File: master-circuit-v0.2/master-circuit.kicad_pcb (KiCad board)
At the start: 4 copper layers, 70 x 86 mm, 254 parts, among them U6 20nF 5%, X2 24MHz

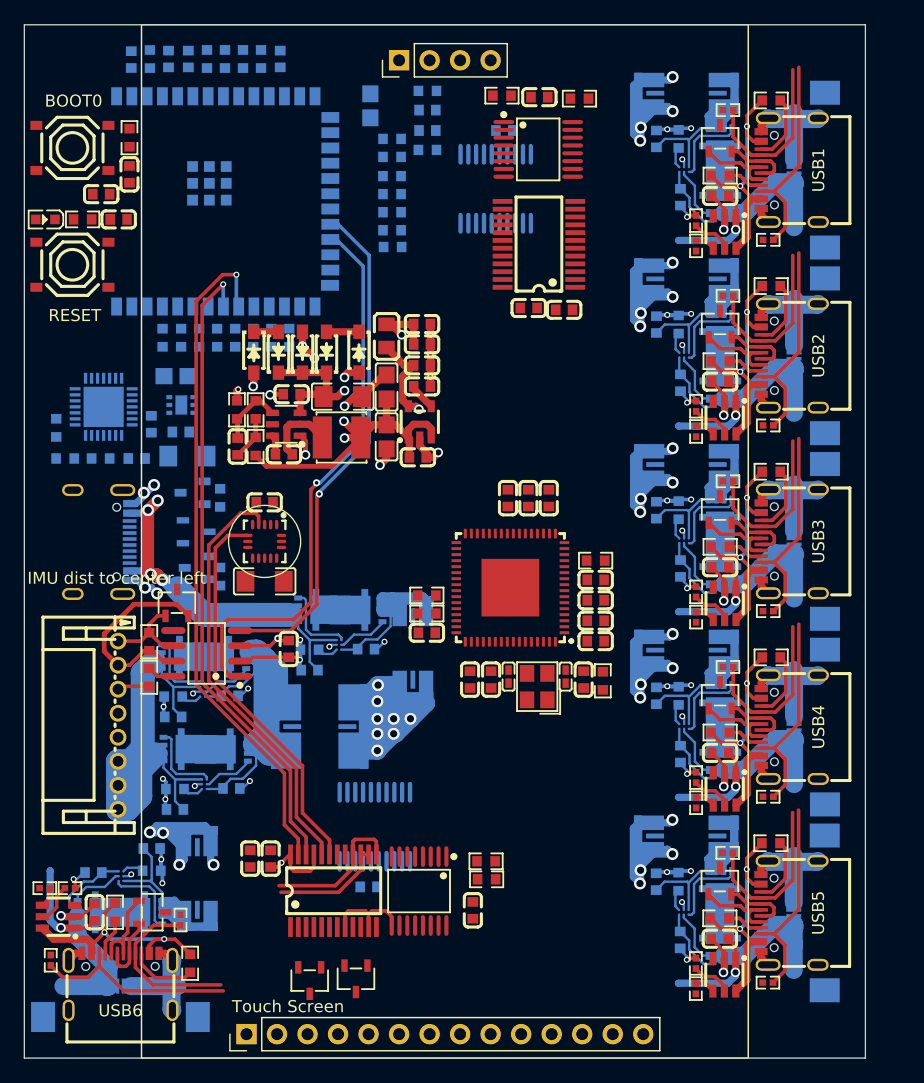
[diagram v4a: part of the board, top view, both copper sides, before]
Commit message: Deal with most of the connection spider web, connector lines remaining.
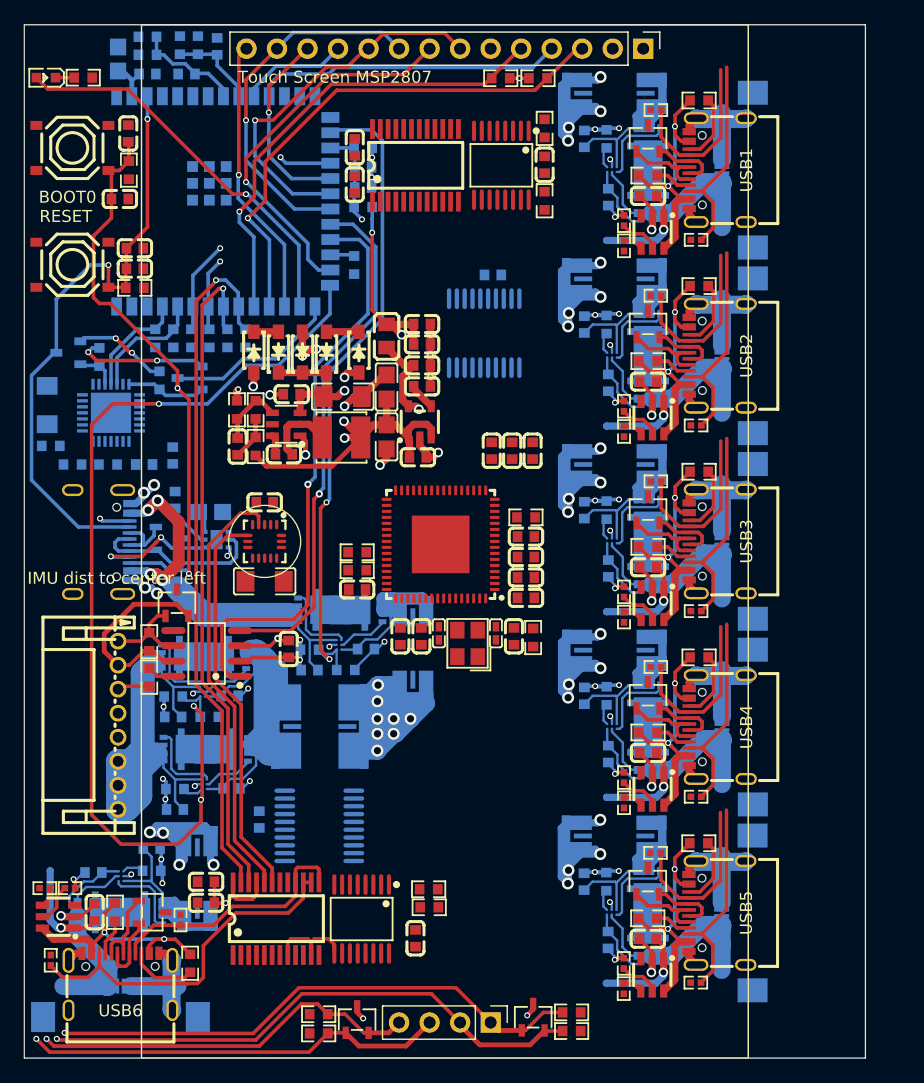
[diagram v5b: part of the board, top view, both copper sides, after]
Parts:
- C1, R14, R15, R26, R27, R34, R37, R9: moved to F.Cu
- moved R9 72.8 mm to (145.6, 139.2)
- moved R34 72.7 mm to (145.6, 140.8)
- moved R15 68.6 mm to (124.5, 140.9), turned to 180 degrees
- moved R14 68.5 mm to (124.5, 139.3), turned to 180 degrees
- moved R12 44.4 mm to (126.8, 110.7)
- moved R11 42.0 mm to (115.4, 114.6)
- moved R27 29.9 mm to (142.8, 61.5), turned to 180 degrees
- moved R26 28.8 mm to (139.7, 61.5), turned to 0 degrees
- moved C3 21.4 mm to (107.8, 59.9), turned to -90 degrees
- moved C84 20.3 mm to (127.5, 70.3), turned to -90 degrees
- moved C42 19.7 mm to (127.5, 67.2), turned to 90 degrees
- moved R37 19.1 mm to (109.2, 78.9), turned to 0 degrees
- moved C1 17.7 mm to (109.2, 77.3), turned to 180 degrees
- moved R43 17.1 mm to (111.2, 86.6)
- moved Q10 15.8 mm to (113.8, 86.4)
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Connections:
- net Net-(Q10-B) renamed /RTS-GATE
- net Net-(Q9-B) renamed /DTR-GATE
- net Net-(U5-VSET) renamed /USB-PD-VSET
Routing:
- net FSPID/SPI2_MOSI: track 0.00 -> 169.5 mm, vias 0 -> 2
- net FSPIQ/SPI2_MISO: track 0.00 -> 154.8 mm, vias 0 -> 2
- net FSPICLK/SPI2_CLK: track 0.00 -> 153.3 mm, vias 0 -> 2
- net FSPICS0/MEMORY_CS: track 0.00 -> 138.4 mm, vias 0 -> 2
- net CONNECT_BATTERY: track 3.57 -> 86.6 mm, vias 0 -> 3
- net BOOT0: track 0.00 -> 62.5 mm, vias 0 -> 2
- net CONNECT_VBUS: track 1.79 -> 55.1 mm, vias 0 -> 2
- net ENABLE-ESP32: track 0.00 -> 51.3 mm, vias 0 -> 2
- net SCREEN_CS: track 0.00 -> 44.2 mm, vias 0 -> 1
- net SCREEN_DC: track 0.00 -> 39.3 mm, vias 0 -> 1
- net STATUS_LED: track 0.00 -> 32.8 mm, vias 0 -> 1
- net SCREEN_LED: track 0.00 -> 31.9 mm, vias 0 -> 1
- net SCREEN_RESET: track 0.00 -> 25.7 mm
- net TOUCH_INT: track 0.00 -> 23.4 mm, vias 0 -> 1
- net CC2: track 0.00 -> 15.6 mm, vias 0 -> 2
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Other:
- board text added: "Touch Screen MSP2807"
- board text removed: "Touch Screen"
